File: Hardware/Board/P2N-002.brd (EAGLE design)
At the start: 72 x 72 mm, 38 parts, among them IC1 4053N, IC2 LTC485N, IC3 74LS07N, IC4 LTC485N, K1 G5V1, T1 2SC1815

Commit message: New layout.
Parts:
- added JP6: (no value), pinhead:1X03
- JP2: device pinhead:1X05/90 -> pinhead:1X04
- JP3: device pinhead:1X04 -> pinhead:1X14
- JP4: device pinhead:1X03 -> pinhead:1X02
- JP5: device pinhead:1X14 -> pinhead:1X05/90
- moved JP2 71.2 mm to (52.0, 11.0)
- moved JP5 57.1 mm to (0.00, 59.7)
- moved JP3 25.0 mm to (52.0, 36.0)
- moved JP4 12.8 mm to (8.89, 17.8), turned to 90 degrees
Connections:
- new net N$30: JP4.1, MC1.P$4
- new net N$31: JP4.2, MC1.P$3
- net ANLG0: now also JP3.8; no longer JP5.8
- net ANLG1: now also JP3.9; no longer JP5.9
- net ANLG2: now also JP3.10; no longer JP5.10
- net ANLG3: now also JP3.11; no longer JP5.11
- net GND: now also JP3.14, JP5.5, R3.2, R4.2; no longer JP2.5, JP3.4, JP5.14, JP5.2
- net MIDI14: no longer MC1.P$9
- net MIDIRX: now also JP6.1; no longer JP4.1
- net N$17: now also JP2.2; no longer JP3.1
- net N$18: now also JP2.4; no longer JP3.3
- net N$20: now also JP2.1; no longer R3.2
- net N$21: now also JP2.3; no longer R4.2
- net N$22: now also MC1.P$1; no longer MC1.P$5
- net N$24: now also JP3.5, JP5.1, MC1.P$5; no longer JP2.1, JP5.5, MC1.P$3
- net N$25: now also JP3.4, JP5.2; no longer JP2.2, JP5.4
- net N$26: now also JP3.3; no longer JP2.3
- net N$27: now also JP3.6, MC1.P$7; no longer JP5.6, MC1.P$4
- net N$28: now also JP3.12; no longer JP5.12
- net N$29: now also JP3.13; no longer JP5.13
- net N$7: now also JP6.2; no longer JP4.2
- net N$9: now also MC1.P$9; no longer MC1.P$7
- net VCC: now also JP3.7; no longer JP5.7
- net VDD: now also JP3.1; no longer JP5.1
- net XMIDIRX: now also JP6.3; no longer JP4.3
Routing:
- net N$20: track 18.5 -> 112.4 mm, vias 0 -> 3
- net N$21: track 32.0 -> 116.0 mm, vias 1 -> 2
- net N$19: track 155.8 -> 74.5 mm, vias 0 -> 3
- net MIDI14: track 118.5 -> 37.9 mm, vias 4 -> 2
- net N$12: track 76.9 -> 155.6 mm, vias 0 -> 3
- net N$23: track 72.3 -> 137.7 mm, vias 2 -> 4
- net MIDI11: track 61.1 -> 121.5 mm, vias 1 -> 0
- net N$10: track 92.9 -> 145.4 mm
- net N$9: track 48.7 -> 98.3 mm, vias 0 -> 5
- net N$30: track 0.00 -> 48.0 mm
- net GND: track 350.8 -> 304.9 mm, vias 0 -> 3
- net N$31: track 0.00 -> 44.7 mm, vias 0 -> 3
- net VCC: track 213.5 -> 256.6 mm, vias 1 -> 3
- net MIDI13: track 105.4 -> 136.2 mm, vias 1 -> 2
- net MIDI6: track 59.2 -> 36.7 mm, vias 1 -> 0
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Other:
- board text added: "JP2: TXA/TXK/RXA/RXK JP5: VBUS/D-/D+/NC/GND CN1: TX+/TX-/RX+/RX-"
- board text removed: "JP2: VBUS/D-/D+/NC/GND JP3: TXA/TXK/RXA/RXK CN1: TX+/TX-/RX+/RX-"

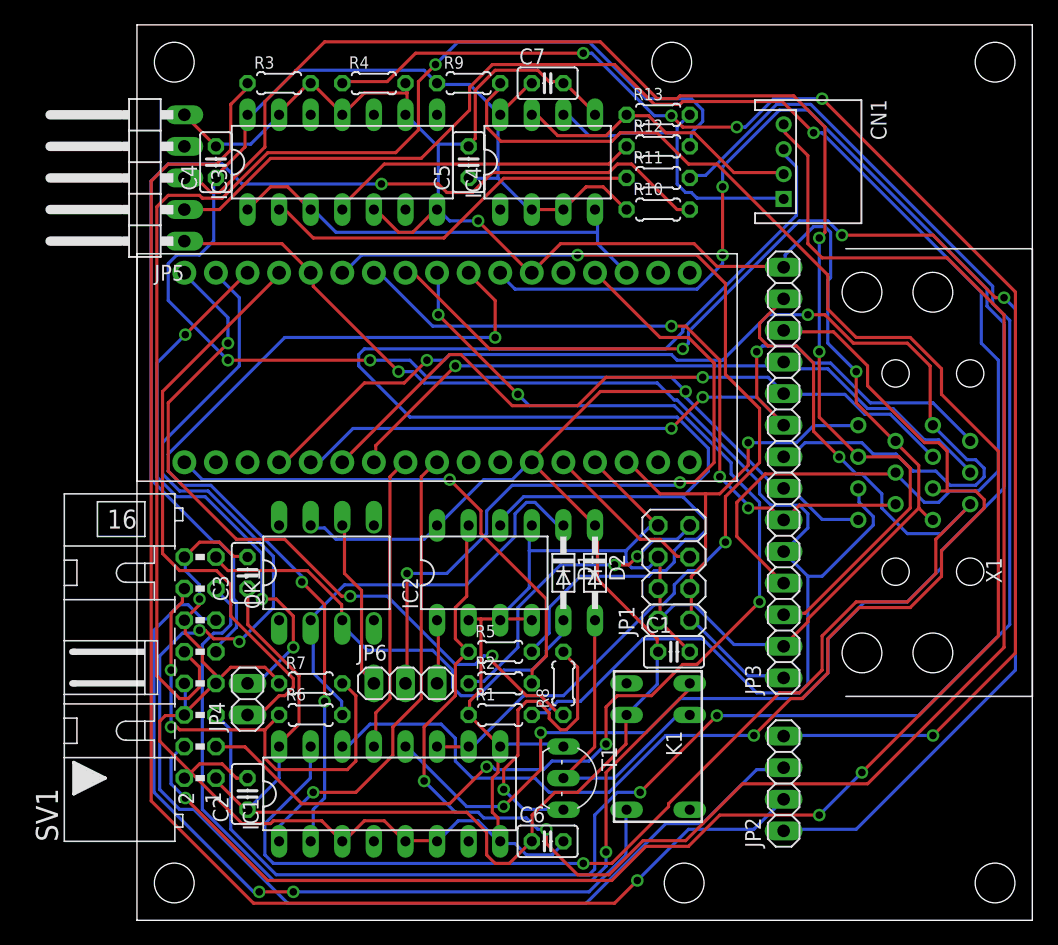
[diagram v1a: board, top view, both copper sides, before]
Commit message: Changed MIDI IN/OUT layout.
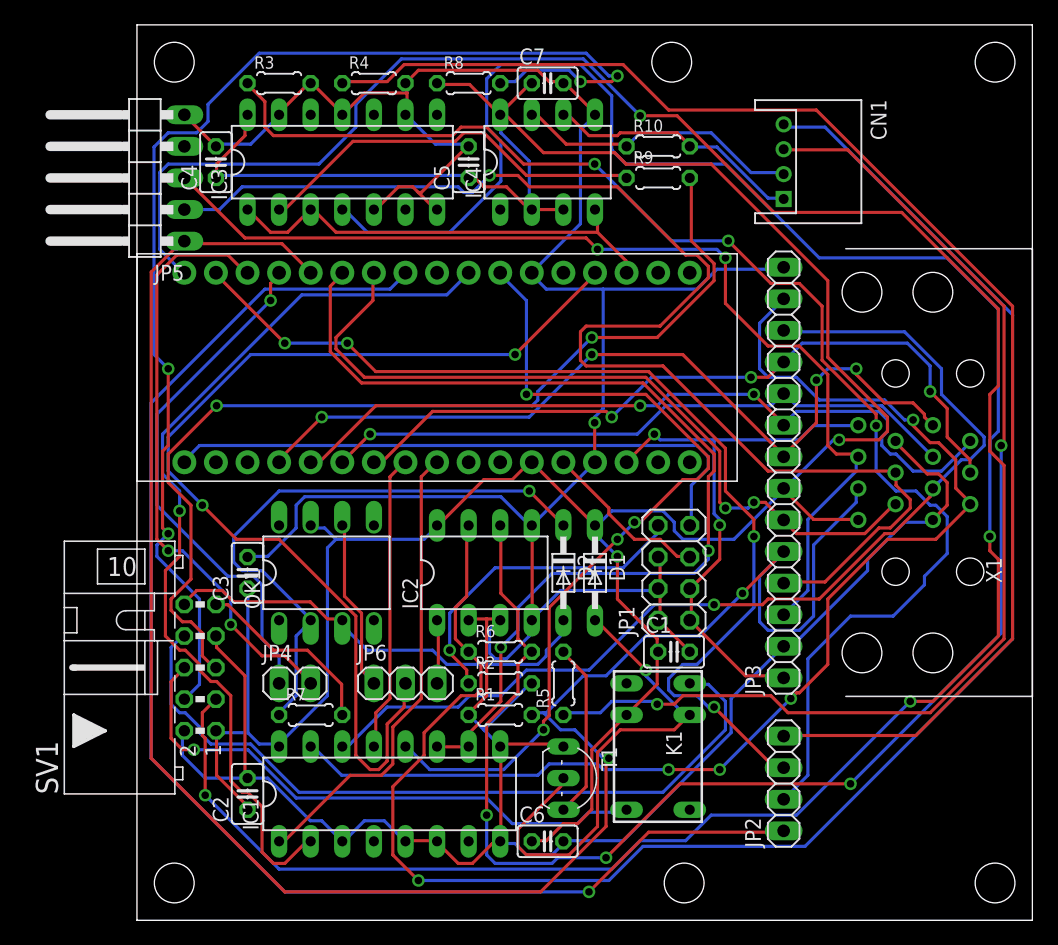
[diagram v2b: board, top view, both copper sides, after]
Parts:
- removed R11, R12: 220, resistor:0204/5
- removed R13: 120, resistor:0204/5
- R10, R6: value 220 -> 120
- R5: value 120 -> 3.3k
- R7: value 10k -> 220
- R8: value 3.3k -> 220
- SV1: device con-ml:ML16L -> con-ml:ML10L
- moved R8 48.9 mm to (26.7, 67.3), turned to 0 degrees
- moved R9 17.0 mm to (41.9, 59.7)
- moved R6 16.1 mm to (29.2, 21.6)
- moved R5 5.68 mm to (34.3, 19.1), turned to 90 degrees
- moved R10 5.08 mm to (41.9, 62.2)
- moved JP4 4.02 mm to (12.7, 19.1), turned to 0 degrees
- moved D1 2.54 mm to (36.8, 27.9)
- moved D2 2.54 mm to (34.3, 27.9)
- moved R7 2.54 mm to (14.0, 16.5)
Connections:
- removed net MIDI14: R6.1, R7.2, SV1.14
- removed net N$11: R10.2, SV1.9
- removed net N$13: R12.2, SV1.10
- removed net N$9: MC1.P$9, SV1.3
- new net N$32: JP1.8, R2.1
- net GND: now also R2.2; no longer JP1.8, R7.1, SV1.12, SV1.16, SV1.6, SV1.8
- net MIDI1: now also R10.2; no longer R13.2
- net MIDI11: now also R6.2; no longer R5.2
- net MIDI13: now also R6.1; no longer R5.1
- net MIDI15: now also D2.A, SV1.10; no longer D1.A, SV1.15
- net MIDI3: now also R10.1; no longer R13.1
- net N$1: now also SV1.3; no longer R12.1
- net N$10: now also R9.2; no longer R11.2
- net N$12: now also R8.2; no longer R9.2
- net N$14: now also SV1.8; no longer SV1.13
- net N$15: now also D2.C, R7.1; no longer D1.C, R6.2
- net N$16: now also SV1.6; no longer SV1.11
- net N$2: now also R9.1; no longer R11.1
- net N$22: now also R5.1; no longer R8.1
- net N$4: now also MC1.P$34; no longer R2.1
- net N$5: now also R7.2, SV1.9; no longer MC1.P$34, R2.2
- net N$6: now also D1.A; no longer D2.A
- net N$8: now also R5.2; no longer R8.2
- net VCC: now also D1.C, R8.1; no longer D2.C, R10.1, R9.1
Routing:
- net N$1: track 25.2 -> 185.4 mm, vias 0 -> 3
- net N$13: track 103.1 -> 0.00 mm, vias 1 -> 0
- net N$9: track 98.3 -> 0.00 mm, vias 5 -> 0
- net N$22: track 60.2 -> 156.2 mm, vias 3 -> 2
- net N$11: track 89.1 -> 0.00 mm, vias 1 -> 0
- net N$23: track 137.7 -> 68.9 mm
- net N$10: track 145.4 -> 79.8 mm
- net N$12: track 155.6 -> 100.0 mm, vias 3 -> 4
- net N$24: track 113.0 -> 158.7 mm, vias 1 -> 2
- net MIDI14: track 37.9 -> 0.00 mm, vias 2 -> 0
- net N$21: track 116.0 -> 82.6 mm, vias 2 -> 4
- net N$26: track 111.7 -> 84.3 mm
- net N$5: track 42.0 -> 15.2 mm, vias 1 -> 0
- net N$32: track 0.00 -> 26.3 mm, vias 0 -> 1
- net N$7: track 58.9 -> 83.9 mm
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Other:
- board text removed: "JP2: TXA/TXK/RXA/RXK JP5: VBUS/D-/D+/NC/GND CN1: TX+/TX-/RX+/RX-"

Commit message: Internal drive port.
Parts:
- removed C6, C7: 103, rcl:C025-025X050
- removed JP6: (no value), pinhead:1X03
- added S1: TL36PO, switch:TL3XPO
- JP4: device pinhead:1X02 -> pinhead:2X03
- moved R8 53.0 mm to (11.4, 16.5)
- moved R3 32.1 mm to (41.9, 57.1)
- moved R1 27.5 mm to (6.35, 31.8)
- moved R4 24.1 mm to (41.9, 59.7)
- moved C2 17.8 mm to (8.89, 27.9)
- moved C1 17.0 mm to (35.6, 6.35)
- moved C3 12.7 mm to (21.6, 27.9)
- moved JP4 11.4 mm to (7.62, 8.89), turned to 90 degrees
- moved R6 5.68 mm to (34.3, 19.1), turned to 90 degrees
- moved R7 3.59 mm to (11.4, 19.1)
- moved R10 2.54 mm to (41.9, 64.8)
- moved R2 2.54 mm to (31.8, 19.1), turned to 90 degrees
- moved R5 2.54 mm to (36.8, 19.1)
- moved R9 2.54 mm to (41.9, 62.2)
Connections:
- new net N$11: JP4.5, MC1.P$17
- new net N$13: JP4.6, MC1.P$18
- new net N$33: JP4.4, MC1.P$19
- new net N$9: JP4.3, MC1.P$9
- net GND: no longer C6.2, C7.2
- net MIDIRX: now also S1.1; no longer JP6.1
- net N$7: now also S1.2; no longer JP6.2
- net VCC: no longer C6.1, C7.1
- net XMIDIRX: now also S1.3; no longer JP6.3
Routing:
- net N$11: track 0.00 -> 166.2 mm, vias 0 -> 4
- net N$9: track 0.00 -> 144.5 mm, vias 0 -> 4
- net N$12: track 100.0 -> 11.6 mm, vias 4 -> 0
- net N$22: track 156.2 -> 73.9 mm
- net N$13: track 0.00 -> 76.2 mm, vias 0 -> 3
- net N$33: track 0.00 -> 68.6 mm, vias 0 -> 2
- net N$4: track 49.3 -> 104.7 mm, vias 0 -> 2
- net VDD: track 45.6 -> 93.4 mm
- net N$17: track 107.9 -> 60.6 mm, vias 3 -> 5
- net N$24: track 158.7 -> 114.7 mm, vias 2 -> 1
- net N$30: track 42.4 -> 0.00 mm, vias 1 -> 0
- net N$18: track 110.9 -> 77.4 mm
- net N$20: track 110.7 -> 79.6 mm, vias 1 -> 2
- net N$19: track 73.8 -> 100.2 mm, vias 1 -> 5
- net N$23: track 68.9 -> 93.9 mm, vias 4 -> 6
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
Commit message: Rerouted.
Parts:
- moved R4 48.9 mm to (64.8, 16.5)
- moved R1 46.8 mm to (41.9, 62.2)
- moved R3 43.4 mm to (57.1, 16.5)
- moved R10 5.08 mm to (41.9, 59.7)
- moved R9 5.08 mm to (41.9, 57.1)
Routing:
- net N$1: track 183.1 -> 61.1 mm, vias 3 -> 1
- net N$18: track 77.4 -> 10.9 mm
- net N$10: track 79.8 -> 143.2 mm, vias 3 -> 4
- net N$4: track 104.7 -> 48.1 mm
- net N$30: track 0.00 -> 53.3 mm
- net N$17: track 60.6 -> 7.94 mm, vias 5 -> 0
- net N$29: track 94.6 -> 142.8 mm, vias 0 -> 4
- net VDD: track 93.4 -> 48.2 mm, vias 2 -> 0
- net ANLG2: track 53.1 -> 95.3 mm, vias 2 -> 3
- net N$21: track 79.7 -> 118.1 mm, vias 2 -> 3
- net N$11: track 166.2 -> 133.1 mm, vias 4 -> 3
- net N$20: track 79.6 -> 111.3 mm
- net ANLG0: track 87.7 -> 58.9 mm, vias 2 -> 1
- net N$7: track 98.1 -> 70.2 mm, vias 3 -> 2
- net N$23: track 93.9 -> 67.9 mm, vias 6 -> 2
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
